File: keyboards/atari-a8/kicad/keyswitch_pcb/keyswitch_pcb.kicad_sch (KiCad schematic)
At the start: 25 parts, among them J101 PLAYER 1, J102 Development Connector, J103 I2C DISPLAY, J104 Jumper Connector, J105 Primary Connector, SW101 RESET, U101 MAX7219, U102 MAX7219

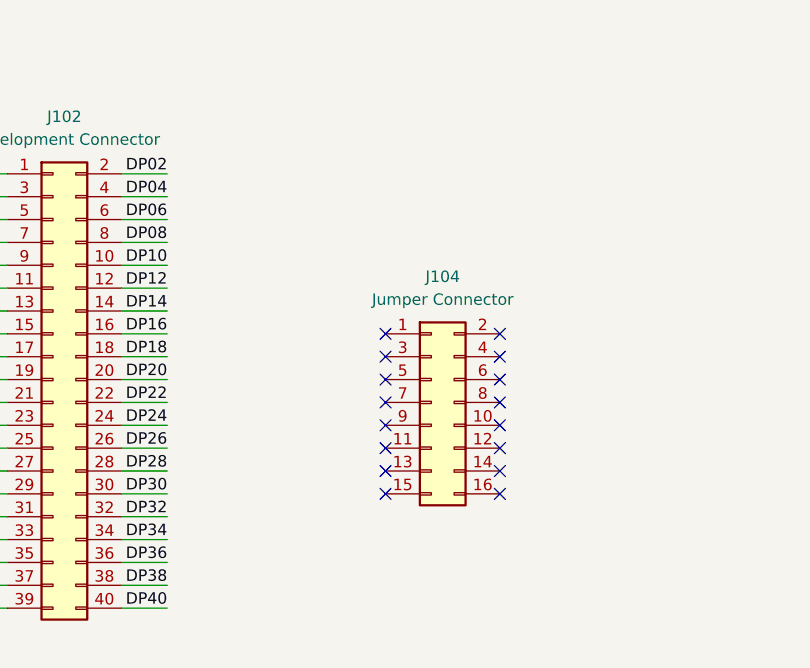
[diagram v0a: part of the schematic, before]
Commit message: Reworked mounting holes and cleaned up labeling.
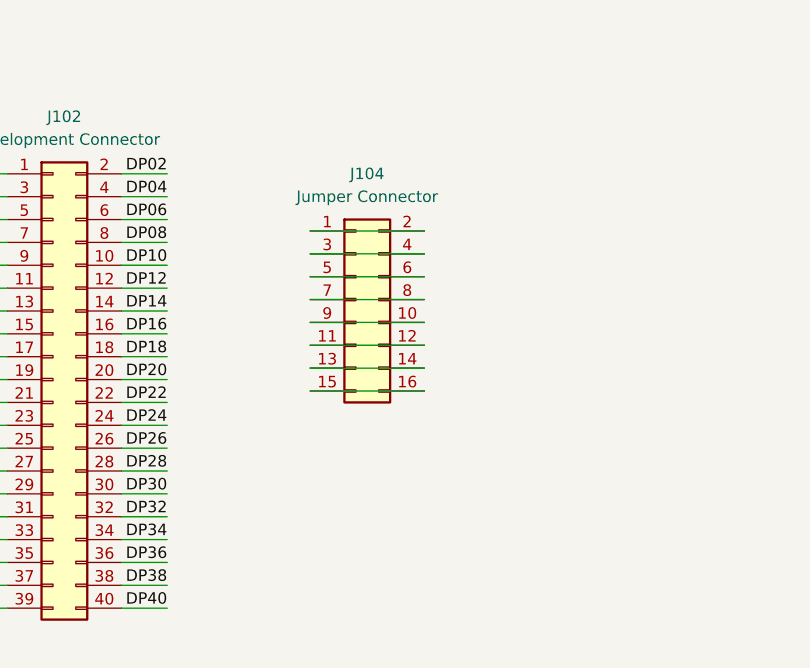
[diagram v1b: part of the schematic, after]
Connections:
- net at J104.1 (Pin_1): now also J104.2 (Pin_2)
- net at J104.10 (Pin_10): now also J104.9 (Pin_9)
- net at J104.11 (Pin_11): now also J104.12 (Pin_12)
- net at J104.13 (Pin_13): now also J104.14 (Pin_14)
- net at J104.15 (Pin_15): now also J104.16 (Pin_16)
- net at J104.3 (Pin_3): now also J104.4 (Pin_4)
- net at J104.5 (Pin_5): now also J104.6 (Pin_6)
- net at J104.7 (Pin_7): now also J104.8 (Pin_8)
- no-connect marks 33 -> 17
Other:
- moved on the sheet: J104
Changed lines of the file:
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@@
   (junction (at 268.224 17.018) (diameter 0) (color 0 0 0 0)
   )
-  (no_connect (at 122.682 128.27))
-  (no_connect (at 135.382 135.89))
   (no_connect (at 213.614 74.168))
-  (no_connect (at 122.682 133.35))
   (no_connect (at 213.614 86.868))
   (no_connect (at 120.65 74.93))
-  (no_connect (at 122.682 123.19))
   (no_connect (at 120.65 72.39))
-  (no_connect (at 135.382 120.65))
   (no_connect (at 213.614 69.088))
   (no_connect (at 213.614 53.848))
-  (no_connect (at 122.682 135.89))
   (no_connect (at 213.614 79.248))
   (no_connect (at 213.614 56.388))
-  (no_connect (at 135.382 125.73))
-  (no_connect (at 135.382 133.35))
-  (no_connect (at 135.382 130.81))
   (no_connect (at 213.614 81.788))
-  (no_connect (at 122.682 120.65))
   (no_connect (at 213.614 46.228))
-  (no_connect (at 135.382 128.27))
   (no_connect (at 213.614 51.308))
-  (no_connect (at 135.382 118.11))
   (no_connect (at 213.614 48.768))
-  (no_connect (at 122.682 125.73))
   (no_connect (at 213.614 61.468))
   (no_connect (at 213.614 58.928))
@@
   (no_connect (at 213.614 84.328))
   (no_connect (at 213.614 76.708))
-  (no_connect (at 122.682 118.11))
-  (no_connect (at 135.382 123.19))
-  (no_connect (at 122.682 130.81))
   (wire (pts (xy 100.33 57.15) (xy 101.6 57.15))
     (stroke (width 0) (type default))
@@
     (stroke (width 0) (type default))
   )
+  (wire (pts (xy 114.3 124.46) (xy 127 124.46))
+    (stroke (width 0) (type default))
+  )
   (wire (pts (xy 93.345 148.59) (xy 98.425 148.59))
     (stroke (width 0) (type default))
@@
     (stroke (width 0) (type default))
   )
+  (wire (pts (xy 114.3 111.76) (xy 127 111.76))
+    (stroke (width 0) (type default))
+  )
   (wire (pts (xy 211.074 22.098) (xy 211.074 23.368))
     (stroke (width 0) (type default))
@@
     (stroke (width 0) (type default))
   )
+  (wire (pts (xy 114.3 114.3) (xy 127 114.3))
+    (stroke (width 0) (type default))
+  )
   (wire (pts (xy 27.94 124.46) (xy 33.655 124.46))
     (stroke (width 0) (type default))
@@
     (stroke (width 0) (type default))
   )
+  (wire (pts (xy 114.3 119.38) (xy 127 119.38))
+    (stroke (width 0) (type default))
+  )
   (wire (pts (xy 74.93 102.87) (xy 80.645 102.87))
     (stroke (width 0) (type default))
@@
     (stroke (width 0) (type default))
   )
+  (wire (pts (xy 114.3 106.68) (xy 127 106.68))
+    (stroke (width 0) (type default))
+  )
   (wire (pts (xy 100.33 54.61) (xy 101.6 54.61))
     (stroke (width 0) (type default))
@@
     (stroke (width 0) (type default))
   )
+  (wire (pts (xy 114.3 109.22) (xy 127 109.22))
+    (stroke (width 0) (type default))
+  )
   (wire (pts (xy 27.94 106.68) (xy 33.655 106.68))
     (stroke (width 0) (type default))
   )
+  (wire (pts (xy 114.3 121.92) (xy 127 121.92))
+    (stroke (width 0) (type default))
+  )
   (wire (pts (xy 100.33 52.07) (xy 120.65 52.07))
     (stroke (width 0) (type default))
@@
   )
   (wire (pts (xy 46.355 106.68) (xy 52.705 106.68))
+    (stroke (width 0) (type default))
+  )
+  (wire (pts (xy 114.3 116.84) (xy 127 116.84))
     (stroke (width 0) (type default))
   )
@@
     )
   )
-  (symbol (lib_id "Connector_Generic:Conn_02x08_Odd_Even") (at 127.762 125.73 0) (unit 1)
+  (symbol (lib_id "Connector_Generic:Conn_02x08_Odd_Even") (at 119.38 114.3 0) (unit 1)
     (in_bom yes) (on_board yes) (dnp no) (fields_autoplaced)
-    (property "Reference" "J104" (at 129.032 111.76 0)
+    (property "Reference" "J104" (at 120.65 100.33 0)
       (effects (font (size 1.27 1.27)))
     )
-    (property "Value" "Jumper Connector" (at 129.032 114.3 0)
+    (property "Value" "Jumper Connector" (at 120.65 102.87 0)
       (effects (font (size 1.27 1.27)))
     )
-    (property "Footprint" "Connector_PinSocket_2.54mm:PinSocket_2x08_P2.54mm_Vertical" (at 127.762 125.73 0)
-      (effects (font (size 1.27 1.27)) hide)
-    )
-    (property "Datasheet" "~" (at 127.762 125.73 0)
-      (effects (font (size 1.27 1.27)) hide)
-    )
+    (property "Footprint" "Connector_PinSocket_2.54mm:PinSocket_2x08_P2.54mm_Vertical" (at 119.38 114.3 0)
+      (effects (font (size 1.27 1.27)) hide)
+    )
+    (property "Datasheet" "~" (at 119.38 114.3 0)
+      (effects (font (size 1.27 1.27)) hide)
+    )
